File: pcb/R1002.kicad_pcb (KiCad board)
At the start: 2 copper layers, 45 x 33.3 mm, 26 parts, among them J1 PCIEXPRESS-X1, J2 CONN_01X04, J3 CONN_01X04, Q1 Q_NMOS_GDSD, Q2 Q_NMOS_GDSD, Q3 Q_NMOS_GDSD, Q4 Q_NMOS_GDSD, U1 MC14504B-TSSOP, U2 EFM8BB10F2G

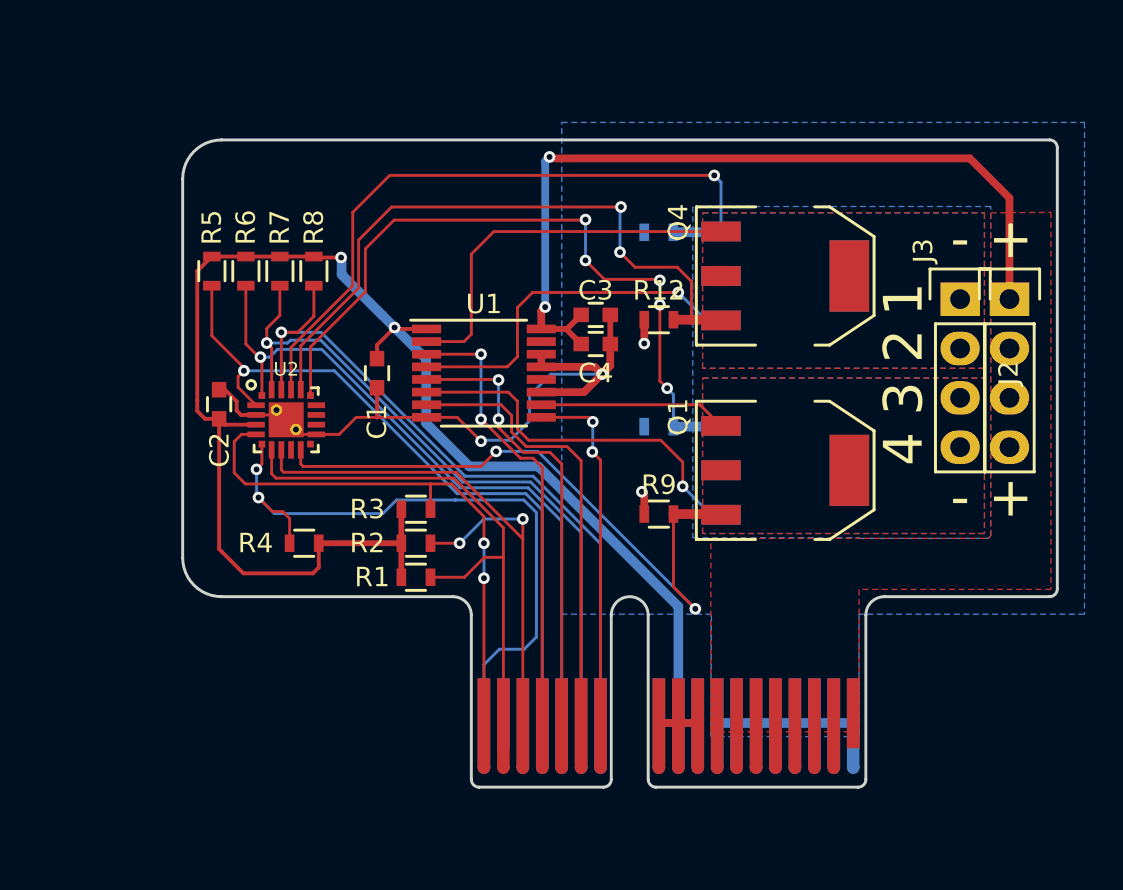
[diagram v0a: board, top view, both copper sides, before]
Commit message: fixed R1002 layout, placed components on the correct side
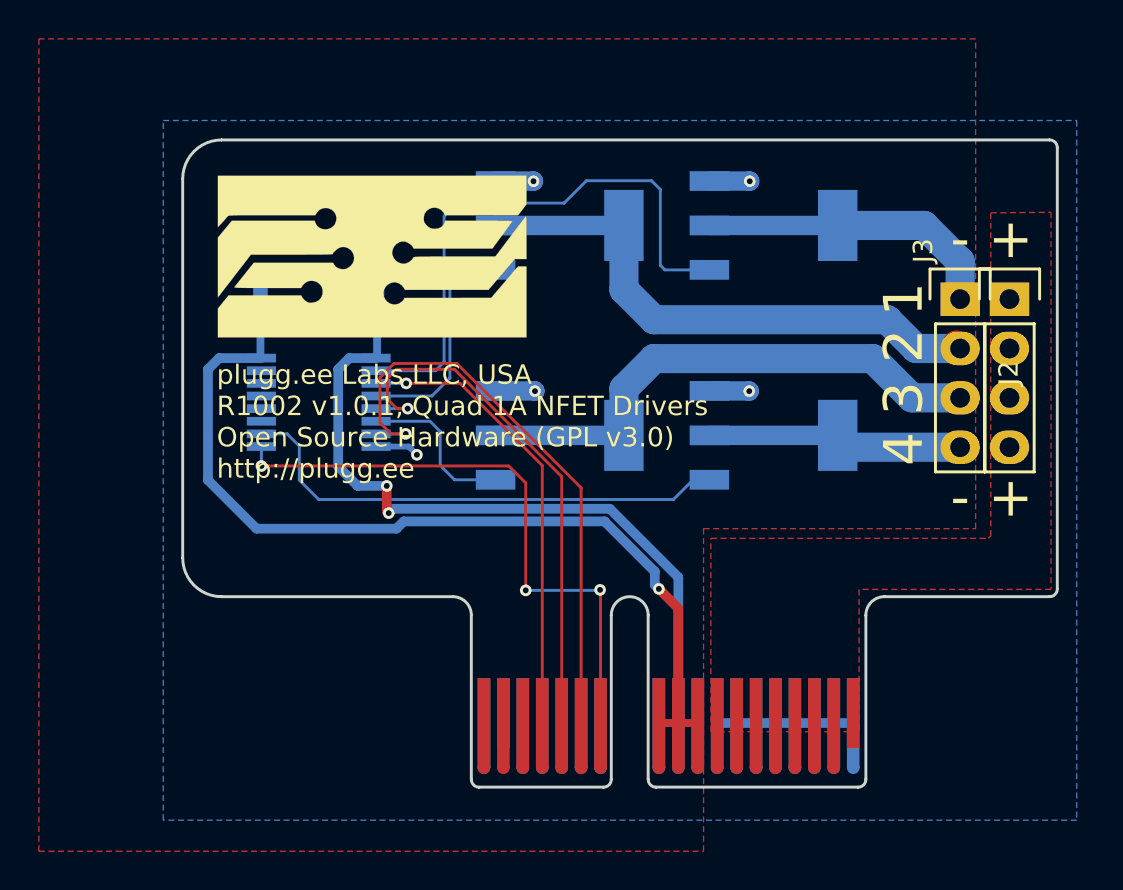
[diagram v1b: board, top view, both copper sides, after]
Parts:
- removed C2, C4: 0.1uF, Capacitors_SMD:C_0603
- removed G***: LOGO, pluggee:pluggee-QRNEG-085X085
- removed R1, R2, R3, R4, R5, R6, R7, R8: 10k, Resistors_SMD:R_0603
- removed R10, R11, R12, R9: 0.1, Resistors_SMD:R_0603
- removed U2: EFM8BB10F2G, Main:QFN50P300X300X75-20NT170X170
- added A1: ART, pluggee:pluggeeLabsIcon-16X8, F.Cu at (134.8, 76.0)
- C1, C3, Q1, Q4, U1: moved to B.Cu
- moved C3 17.3 mm to (129.0, 78.4), turned to 90 degrees
- moved Q3 11.9 mm to (144.4, 74.4)
- moved Q2 11.7 mm to (144.4, 85.2)
- moved U1 8.63 mm to (132.0, 83.5), turned to 180 degrees
- moved C1 3.60 mm to (135.0, 78.4), turned to 90 degrees
- moved Q4 2.67 mm to (155.4, 74.4), turned to 90 degrees
- moved Q1 1.90 mm to (155.4, 85.2), turned to 90 degrees
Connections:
- C3 pad 1: HT -> +5V
- Q1 pad 3: /SN4 -> GND
- Q2 pad 3: /SN3 -> GND
- Q3 pad 3: /SN2 -> GND
- Q4 pad 3: /SN1 -> GND
- U1 pad 16: HT -> +5V
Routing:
- net +5V: track 8.91 -> 53.2 mm, vias 0 -> 1
- net HT: track 59.6 -> 16.1 mm, vias 2 -> 0
- net +3V3: track 85.5 -> 46.5 mm
- net /SN3: track 37.3 -> 0.00 mm, vias 5 -> 0
- net ID0: track 39.0 -> 2.30 mm, vias 1 -> 0
- net ID3: track 38.9 -> 2.30 mm, vias 1 -> 0
- net ID1: track 38.2 -> 2.30 mm, vias 1 -> 0
- net ID2: track 38.0 -> 2.30 mm, vias 1 -> 0
- net /SN2: track 35.3 -> 0.00 mm, vias 1 -> 0
- net /SN1: track 34.2 -> 0.00 mm, vias 2 -> 0
- net C2D: track 36.5 -> 2.30 mm, vias 2 -> 0
- net /SN4: track 32.6 -> 0.00 mm, vias 2 -> 0
- net SCL: track 33.0 -> 2.30 mm, vias 2 -> 0
- net /DN2: track 0.00 -> 28.7 mm
- net ~MRESET: track 31.0 -> 2.30 mm, vias 2 -> 0
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- added copper zone on F.Cu, net GND
- removed copper zone on F.Cu, net /DN1
- removed copper zone on B.Cu, net /DN2
- removed copper zone on B.Cu, net /DN3
- removed copper zone on F.Cu, net /DN4
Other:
- board text added: "plugg.ee Labs LLC, USA R1002 v1.0.1, Quad 1A NFET Drivers Open Source Hardware (GPL v3.0) http://plugg.ee"
- board text removed: "R1002 v1.0.0-beta 1A NFET Drivers http://plugg.ee"
- board text removed: "plugg.ee Labs 2016"

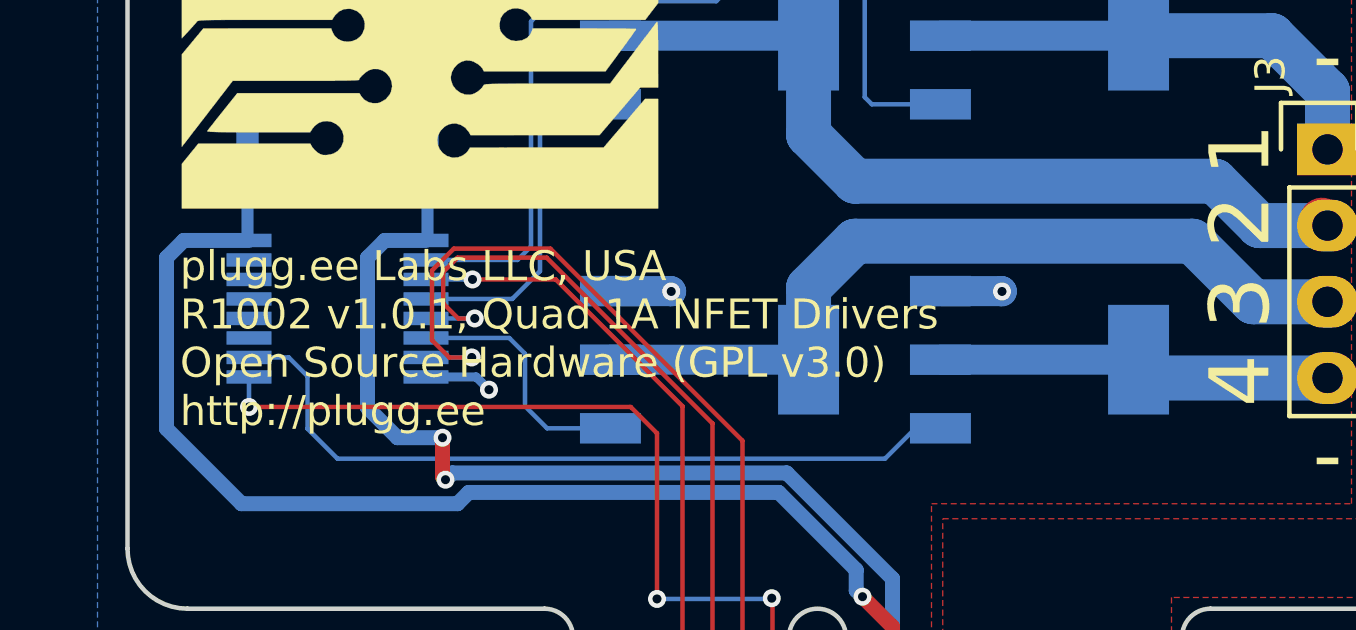
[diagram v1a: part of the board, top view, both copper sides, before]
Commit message: fixed silk screen with v1.1
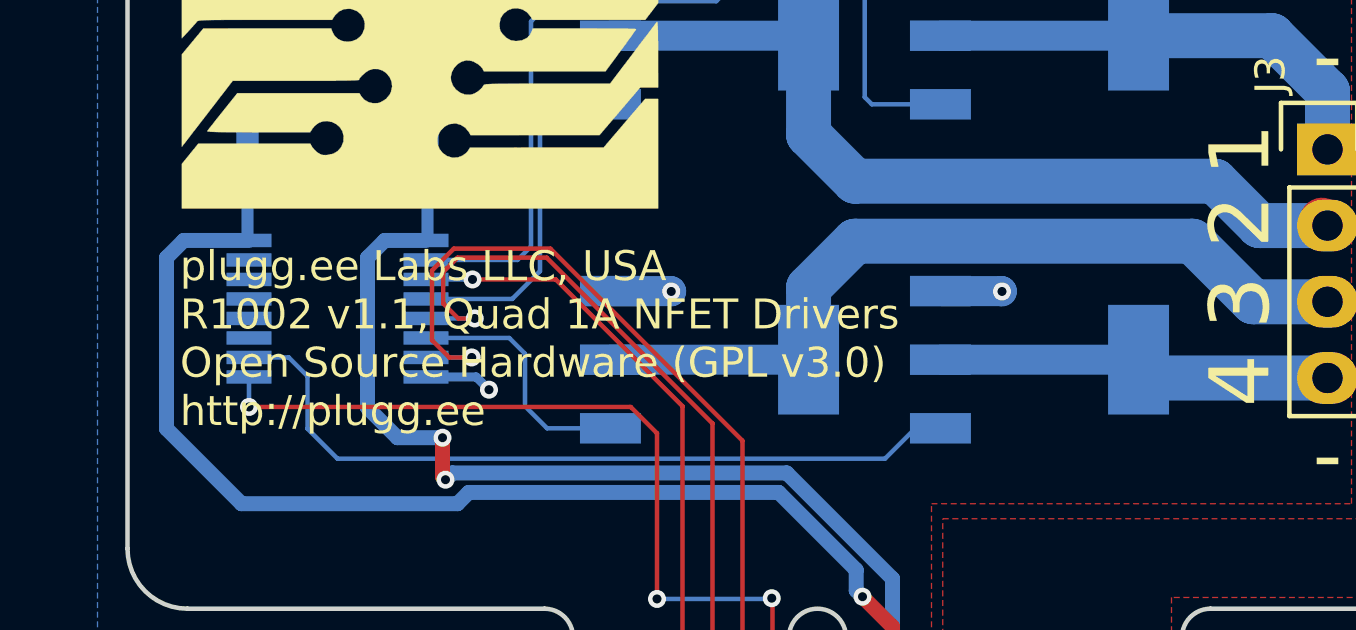
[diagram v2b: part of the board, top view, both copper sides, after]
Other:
- board text added: "plugg.ee Labs LLC, USA R1002 v1.1, Quad 1A NFET Drivers Open Source Hardware (GPL v3.0) http://plugg.ee"
- board text removed: "plugg.ee Labs LLC, USA R1002 v1.0.1, Quad 1A NFET Drivers Open Source Hardware (GPL v3.0) http://plugg.ee"
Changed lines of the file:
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@@
     (links 86)
     (no_connects 0)
-    (area 117.6 64.8 171.000001 106.600001)
+    (area 124.924999 69.924999 170.075001 103.375001)
     (thickness 1.6)
     (drawings 39)
@@
     (35 F.Paste user)
     (36 B.SilkS user)
-    (37 F.SilkS user hide)
+    (37 F.SilkS user)
     (38 B.Mask user hide)
     (39 F.Mask user hide)
@@
     (effects (font (size 2 2) (thickness 0.2)) (justify mirror))
   )
-  (gr_text "plugg.ee Labs LLC, USA\nR1002 v1.0.1, Quad 1A NFET Drivers\nOpen Source Hardware (GPL v3.0)\nhttp://plugg.ee" (at 126.75 84.5) (layer F.SilkS)
+  (gr_text "plugg.ee Labs LLC, USA\nR1002 v1.1, Quad 1A NFET Drivers\nOpen Source Hardware (GPL v3.0)\nhttp://plugg.ee" (at 126.75 84.5) (layer F.SilkS)
     (effects (font (size 1 1) (thickness 0.2)) (justify left))
   )
